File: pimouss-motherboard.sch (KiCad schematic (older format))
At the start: 0 parts

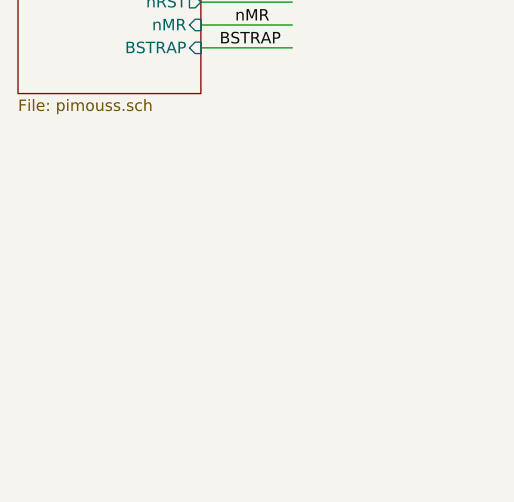
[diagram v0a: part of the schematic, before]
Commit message: sch: Add PCIe power supply
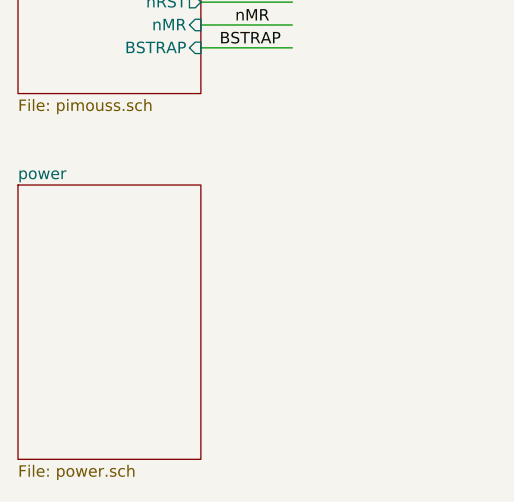
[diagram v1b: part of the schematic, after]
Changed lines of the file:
@@
 $Descr A4 11693 8268
 encoding utf-8
-Sheet 1 9
+Sheet 1 10
 Title "Global motherboard interconnections"
 Date "2019-03-19"
@@
 Text Label 7100 5200 0    50   ~ 0
 SDIO
+$Sheet
+S 2100 4700 800  1200
+U 5D0C4621
+F0 "power" 50
+F1 "power.sch" 50
+$EndSheet
 $EndSCHEMATC

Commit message: sch: Misc fixes
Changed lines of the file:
@@
 Wire Bus Line
 	2900 2600 3300 2600
-Text Label 3250 2600 2    50   ~ 0
+Text Label 3300 2600 2    50   ~ 0
 PCIE_1X
 Wire Bus Line
 	2900 2700 3300 2700
-Text Label 3250 2700 2    50   ~ 0
+Text Label 3300 2700 2    50   ~ 0
 PCIE_4X
 Wire Bus Line
 	2900 2900 3300 2900
-Text Label 3250 2900 2    50   ~ 0
+Text Label 3300 2900 2    50   ~ 0
 QSGMII
 Wire Bus Line
 	3300 3000 2900 3000
-Text Label 3200 3000 2    50   ~ 0
+Text Label 3300 3000 2    50   ~ 0
 MIIM
 Wire Bus Line
 	2900 3200 3300 3200
-Text Label 3200 3200 2    50   ~ 0
+Text Label 3300 3200 2    50   ~ 0
 GPIO
 Wire Bus Line
 	2900 3300 3300 3300
-Text Label 3200 3300 2    50   ~ 0
+Text Label 3300 3300 2    50   ~ 0
 UART
 Wire Bus Line
 	2900 3400 3300 3400
-Text Label 3200 3400 2    50   ~ 0
+Text Label 3300 3400 2    50   ~ 0
 SDIO
 Wire Bus Line
 	2900 3500 3300 3500
-Text Label 3250 3500 2    50   ~ 0
+Text Label 3300 3500 2    50   ~ 0
 SMBUS
 Wire Bus Line
 	2900 3700 3300 3700
-Text Label 3200 3700 2    50   ~ 0
+Text Label 3300 3700 2    50   ~ 0
 JTAG
 Wire Wire Line
@@
 Wire Wire Line
 	3300 4000 2900 4000
-Text Label 3200 3900 2    50   ~ 0
+Text Label 3300 3900 2    50   ~ 0
 nRST
-Text Label 3200 4000 2    50   ~ 0
+Text Label 3300 4000 2    50   ~ 0
 nMR
 Wire Wire Line
 	3300 4100 2900 4100
-Text Label 3250 4100 2    50   ~ 0
+Text Label 3300 4100 2    50   ~ 0
 BSTRAP
 Wire Wire Line
 	6500 2400 7400 2400
-Text Label 6600 2400 0    50   ~ 0
+Text Label 6500 2400 0    50   ~ 0
 nRST
 Wire Bus Line
 	7400 2900 6500 2900
-Text Label 6550 2900 0    50   ~ 0
+Text Label 6500 2900 0    50   ~ 0
 QSGMII
 Text Label 7100 2600 0    50   ~ 0
@@
 Wire Bus Line
 	6500 2500 6900 2500
-Text Label 6600 2500 0    50   ~ 0
+Text Label 6500 2500 0    50   ~ 0
 MIIM
 $Sheet
@@
 Wire Bus Line
 	7400 3500 7000 3500
-Text Label 7100 3500 0    50   ~ 0
+Text Label 7000 3500 0    50   ~ 0
 UART
 Text Label 7100 2700 0    50   ~ 0
@@
 Wire Bus Line
 	7400 4100 7000 4100
-Text Label 7050 4100 0    50   ~ 0
+Text Label 7000 4100 0    50   ~ 0
 PCIE_1X
 Wire Bus Line
 	7400 4200 7000 4200
-Text Label 7050 4200 0    50   ~ 0
+Text Label 7000 4200 0    50   ~ 0
 PCIE_4X
 Wire Bus Line
 	7400 4400 7000 4400
-Text Label 7050 4400 0    50   ~ 0
+Text Label 7000 4400 0    50   ~ 0
 SMBUS
 Wire Wire Line
 	7000 4600 7400 4600
-Text Label 7100 4600 0    50   ~ 0
+Text Label 7000 4600 0    50   ~ 0
 nRST
 $Sheet
@@
 Wire Bus Line
 	7400 5200 7000 5200
-Text Label 7100 5200 0    50   ~ 0
+Text Label 7000 5200 0    50   ~ 0
 SDIO
 $Sheet

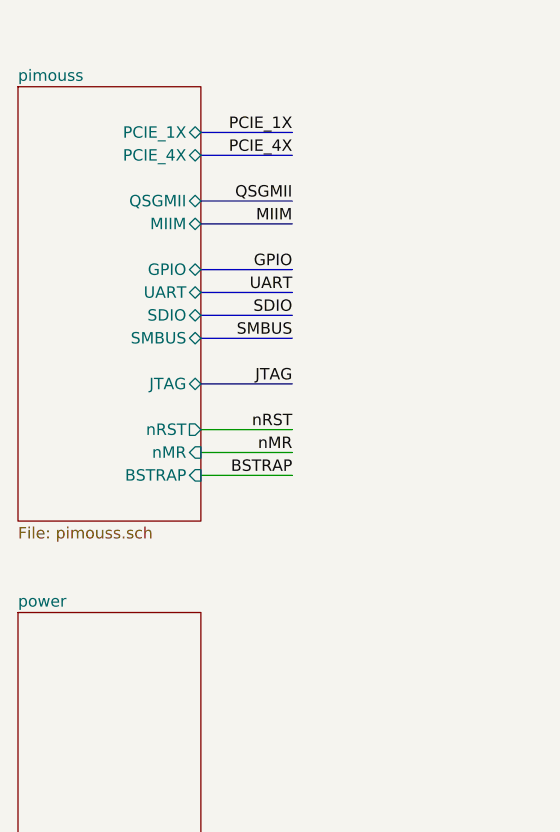
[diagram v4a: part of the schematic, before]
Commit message: sch: Add connectors for JTAG and GPIO
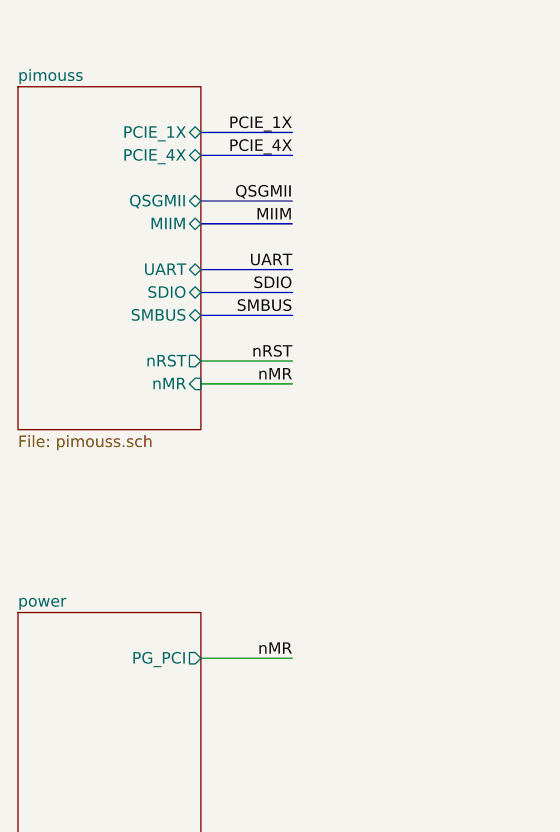
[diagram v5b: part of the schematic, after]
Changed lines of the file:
@@
 F5 "QSGMII" B L 7400 2900 50
-$EndSheet
-$Sheet
-S 2100 2400 800  1900
-U 5CE77C37
-F0 "pimouss" 50
-F1 "pimouss.sch" 50
-F2 "PCIE_1X" B R 2900 2600 50
-F3 "PCIE_4X" B R 2900 2700 50
-F4 "QSGMII" B R 2900 2900 50
-F5 "MIIM" B R 2900 3000 50
-F6 "GPIO" B R 2900 3200 50
-F7 "UART" B R 2900 3300 50
-F8 "SDIO" B R 2900 3400 50
-F9 "SMBUS" B R 2900 3500 50
-F10 "JTAG" B R 2900 3700 50
-F11 "nRST" O R 2900 3900 50
-F12 "nMR" I R 2900 4000 50
-F13 "BSTRAP" I R 2900 4100 50
 $EndSheet
 Wire Bus Line
@@
 	2900 3200 3300 3200
 Text Label 3300 3200 2    50   ~ 0
-GPIO
+UART
 Wire Bus Line
 	2900 3300 3300 3300
 Text Label 3300 3300 2    50   ~ 0
-UART
+SDIO
 Wire Bus Line
 	2900 3400 3300 3400
 Text Label 3300 3400 2    50   ~ 0
-SDIO
-Wire Bus Line
-	2900 3500 3300 3500
-Text Label 3300 3500 2    50   ~ 0
 SMBUS
-Wire Bus Line
-	2900 3700 3300 3700
+Wire Wire Line
+	3300 3600 2900 3600
+Wire Wire Line
+	3300 3700 2900 3700
+Text Label 3300 3600 2    50   ~ 0
+nRST
 Text Label 3300 3700 2    50   ~ 0
-JTAG
-Wire Wire Line
-	3300 3900 2900 3900
-Wire Wire Line
-	3300 4000 2900 4000
-Text Label 3300 3900 2    50   ~ 0
-nRST
-Text Label 3300 4000 2    50   ~ 0
 nMR
-Wire Wire Line
-	3300 4100 2900 4100
-Text Label 3300 4100 2    50   ~ 0
-BSTRAP
 Wire Wire Line
 	6500 2400 7400 2400
@@
 F0 "power" 50
 F1 "power.sch" 50
+F2 "PG_PCI" O R 2900 4900 50
+$EndSheet
+Wire Wire Line
+	3300 4900 2900 4900
+Text Label 3300 4900 2    50   ~ 0
+nMR
+$Sheet
+S 2100 2400 800  1500
+U 5CE77C37
+F0 "pimouss" 50
+F1 "pimouss.sch" 50
+F2 "PCIE_1X" B R 2900 2600 50
+F3 "PCIE_4X" B R 2900 2700 50
+F4 "QSGMII" B R 2900 2900 50
+F5 "MIIM" B R 2900 3000 50
+F6 "UART" B R 2900 3200 50
+F7 "SDIO" B R 2900 3300 50
+F8 "SMBUS" B R 2900 3400 50
+F9 "nRST" O R 2900 3600 50
+F10 "nMR" I R 2900 3700 50
 $EndSheet
 $EndSCHEMATC
